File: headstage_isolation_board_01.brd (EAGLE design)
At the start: 50 x 40.9 mm, 49 parts

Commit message: fix some naming CONNECTOR STILL WRONG- DONT USE YET
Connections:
- net N$1 renamed MISO2+
- net N$14 renamed SCLK-
- net N$15 renamed SCLK+
- net N$16 renamed MOSI-
- net N$17 renamed MOSI+
- net N$18 renamed CS-
- net N$19 renamed CS+
- net N$2 renamed MISO2-
- net N$3 renamed MISO1+
- net N$4 renamed MISO1-
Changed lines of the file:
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@@
 <wire x1="64.77" y1="18.8595" x2="68.072" y2="12.446" width="0" layer="19" extent="1-1"/>
 </signal>
-<signal name="N$1">
+<signal name="MISO2+">
 <contactref element="S1" pad="T5"/>
 <contactref element="U$4" pad="P7"/>
@@
 <wire x1="58.166" y1="35.306" x2="56.5334" y2="35.306" width="0.2032" layer="1"/>
 </signal>
-<signal name="N$2">
+<signal name="MISO2-">
 <contactref element="S1" pad="B5"/>
 <contactref element="U$4" pad="P8"/>
@@
 <wire x1="66.04" y1="20.066" x2="66.04" y2="18.796" width="0.2032" layer="1"/>
 </signal>
-<signal name="N$3">
+<signal name="MISO1+">
 <contactref element="S1" pad="T4"/>
 <contactref element="U$4" pad="P6"/>
@@
 <wire x1="55.118" y1="34.036" x2="56.5334" y2="34.036" width="0.2032" layer="1"/>
 </signal>
-<signal name="N$4">
+<signal name="MISO1-">
 <contactref element="S1" pad="B4"/>
 <contactref element="U$4" pad="P5"/>
@@
 <wire x1="25.5905" y1="17.272" x2="25.527" y2="17.3355" width="0.2032" layer="1"/>
 </signal>
-<signal name="N$14">
+<signal name="SCLK-">
 <contactref element="S1" pad="B2"/>
 <contactref element="U$7" pad="P2"/>
@@
 <wire x1="64.8335" y1="16.256" x2="64.77" y2="16.3195" width="0.2032" layer="1"/>
 </signal>
-<signal name="N$15">
+<signal name="SCLK+">
 <contactref element="S1" pad="T2"/>
 <contactref element="U$7" pad="P1"/>
@@
 <wire x1="58.166" y1="19.304" x2="56.388" y2="21.082" width="0.2032" layer="1"/>
 </signal>
-<signal name="N$16">
+<signal name="MOSI-">
 <contactref element="S1" pad="B3"/>
 <contactref element="U$7" pad="P3"/>
@@
 <wire x1="64.77" y1="17.018" x2="64.77" y2="16.9545" width="0" layer="19" extent="1-1"/>
 </signal>
-<signal name="N$17">
+<signal name="MOSI+">
 <contactref element="S1" pad="T3"/>
 <contactref element="U$7" pad="P4"/>
@@
 <wire x1="57.912" y1="24.892" x2="56.388" y2="24.892" width="0.2032" layer="1"/>
 </signal>
-<signal name="N$18">
+<signal name="CS-">
 <contactref element="S1" pad="B1"/>
 <contactref element="U$8" pad="P3"/>
@@
 <wire x1="64.77" y1="14.986" x2="64.77" y2="15.6845" width="0.2032" layer="1"/>
 </signal>
-<signal name="N$19">
+<signal name="CS+">
 <contactref element="S1" pad="T1"/>
 <contactref element="U$8" pad="P4"/>

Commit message: added correct connector
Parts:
- added S3: RHD2000-CABLE-DAQ-SIDE, RHD2000_eval_board:OMNETICS_PZN-12-AA
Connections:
- net N$10 renamed MISO2-_ISOLATED
- net N$11 renamed MISO1+_ISOLATED
- net N$12 renamed MISO1-V
- net N$13 renamed MISO2+_ISOLATED
- net N$20 renamed CS-_ISOLATED
- net N$21 renamed SCLK-_ISOLATED
- net N$22 renamed SCLK+_ISOLATED
- net N$23 renamed MOSI-_ISOLATED
- net N$24 renamed MOSI+_ISOLATED
- net N$9 renamed CS+_ISOLATED
- new net CCS+: S3.B1
- new net CCS-: S3.T1
- new net CGND: S3.T6
- new net CMISO1+: S3.B4
- new net CMISO1-: S3.T4
- new net CMISO2+: S3.B5
- new net CMISO2-: S3.T5
- new net CMOSI+: S3.B3
- new net CMOSI-: S3.T3
- new net CSCLK+: S3.B2
- new net CSCLK-: S3.T2
- new net CVDD: S3.B6
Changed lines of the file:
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@@
 <layer number="14" name="Route14" color="1" fill="6" visible="no" active="yes"/>
 <layer number="15" name="Route15" color="4" fill="6" visible="no" active="yes"/>
-<layer number="16" name="Bottom" color="9" fill="1" visible="no" active="yes"/>
+<layer number="16" name="Bottom" color="9" fill="1" visible="yes" active="yes"/>
 <layer number="17" name="Pads" color="2" fill="1" visible="no" active="yes"/>
 <layer number="18" name="Vias" color="2" fill="1" visible="no" active="yes"/>
-<layer number="19" name="Unrouted" color="12" fill="1" visible="no" active="yes"/>
+<layer number="19" name="Unrouted" color="12" fill="1" visible="yes" active="yes"/>
 <layer number="20" name="Dimension" color="15" fill="1" visible="yes" active="yes"/>
 <layer number="21" name="tPlace" color="7" fill="1" visible="yes" active="yes"/>
@@
 <element name="C17" library="RHD2000_eval_board" package="0603" value="100n" x="52.07" y="27.178"/>
 <element name="C18" library="RHD2000_eval_board" package="0603" value="100n" x="51.054" y="39.116"/>
+<element name="S3" library="RHD2000_eval_board" package="OMNETICS_PZN-12-AA" value="RHD2000-CABLE-DAQ-SIDE" x="13.208" y="17.78" rot="R90"/>
 </elements>
 <signals>
@@
 <wire x1="37.084" y1="34.036" x2="36.188" y2="34.036" width="0.2032" layer="1"/>
 </signal>
-<signal name="N$10">
+<signal name="MISO2-_ISOLATED">
 <contactref element="S2" pad="B5"/>
 <contactref element="U$6" pad="P1"/>
@@
 <wire x1="27.178" y1="26.924" x2="27.178" y2="33.782" width="0.2032" layer="1"/>
 </signal>
-<signal name="N$11">
+<signal name="MISO1+_ISOLATED">
 <contactref element="U$6" pad="P3"/>
 <contactref element="S2" pad="T4"/>
@@
 <wire x1="32.258" y1="34.036" x2="30.988" y2="34.036" width="0.2032" layer="1"/>
 </signal>
-<signal name="N$12">
+<signal name="MISO1-V">
 <contactref element="U$6" pad="P4"/>
 <contactref element="S2" pad="B4"/>
@@
 <wire x1="28.702" y1="32.766" x2="30.988" y2="32.766" width="0.2032" layer="1"/>
 </signal>
-<signal name="N$13">
+<signal name="MISO2+_ISOLATED">
 <contactref element="S2" pad="T5"/>
 <contactref element="U$6" pad="P2"/>
@@
 <wire x1="62.9285" y1="14.986" x2="63.627" y2="15.6845" width="0.2032" layer="1"/>
 </signal>
-<signal name="N$9">
+<signal name="CS+_ISOLATED">
 <contactref element="S2" pad="T1"/>
 <contactref element="U$9" pad="P7"/>
@@
 <wire x1="31.496" y1="16.256" x2="30.868" y2="16.256" width="0" layer="19" extent="1-1"/>
 </signal>
-<signal name="N$20">
+<signal name="CS-_ISOLATED">
 <contactref element="S2" pad="B1"/>
 <contactref element="U$9" pad="P8"/>
@@
 <wire x1="37.084" y1="16.256" x2="36.068" y2="16.256" width="0.2032" layer="1"/>
 </signal>
-<signal name="N$21">
+<signal name="SCLK-_ISOLATED">
 <contactref element="S2" pad="B2"/>
 <contactref element="U$5" pad="P5"/>
@@
 <wire x1="24.3205" y1="19.304" x2="24.384" y2="19.2405" width="0.2032" layer="1"/>
 </signal>
-<signal name="N$22">
+<signal name="SCLK+_ISOLATED">
 <contactref element="U$5" pad="P6"/>
 <contactref element="S2" pad="T2"/>
@@
 <wire x1="25.5905" y1="19.304" x2="25.527" y2="19.2405" width="0.2032" layer="1"/>
 </signal>
-<signal name="N$23">
+<signal name="MOSI-_ISOLATED">
 <contactref element="U$5" pad="P8"/>
 <contactref element="S2" pad="B3"/>
@@
 <wire x1="23.9395" y1="18.542" x2="24.384" y2="18.6055" width="0.2032" layer="1"/>
 </signal>
-<signal name="N$24">
+<signal name="MOSI+_ISOLATED">
 <contactref element="U$5" pad="P7"/>
 <contactref element="S2" pad="T3"/>
@@
 <signal name="N$31">
 </signal>
+<signal name="CCS-">
+<contactref element="S3" pad="T1"/>
+</signal>
+<signal name="CCS+">
+<contactref element="S3" pad="B1"/>
+</signal>
+<signal name="CSCLK-">
+<contactref element="S3" pad="T2"/>
+</signal>
+<signal name="CSCLK+">
+<contactref element="S3" pad="B2"/>
+</signal>
+<signal name="CMOSI-">
+<contactref element="S3" pad="T3"/>
+</signal>
+<signal name="CMOSI+">
+<contactref element="S3" pad="B3"/>
+</signal>
+<signal name="CMISO1-">
+<contactref element="S3" pad="T4"/>
+</signal>
+<signal name="CMISO1+">
+<contactref element="S3" pad="B4"/>
+</signal>
+<signal name="CMISO2-">
+<contactref element="S3" pad="T5"/>
+</signal>
+<signal name="CMISO2+">
+<contactref element="S3" pad="B5"/>
+</signal>
+<signal name="CGND">
+<contactref element="S3" pad="T6"/>
+</signal>
+<signal name="CVDD">
+<contactref element="S3" pad="B6"/>
+</signal>
 </signals>

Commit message: routed correct headstage connector
and some other fixes.
Still lacking testpoints
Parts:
- removed S2: RHD2000-CABLE-AMP-SIDE, RHD2000:OMNETICS_PZN-12-AA
- moved S3 9.40 mm to (22.6, 17.5)
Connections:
- removed net CCS+: S3.B1
- removed net CCS-: S3.T1
- removed net CGND: S3.T6
- removed net CMISO1+: S3.B4
- removed net CMISO1-: S3.T4
- removed net CMISO2+: S3.B5
- removed net CMISO2-: S3.T5
- removed net CMOSI+: S3.B3
- removed net CMOSI-: S3.T3
- removed net CSCLK+: S3.B2
- removed net CSCLK-: S3.T2
- removed net CVDD: S3.B6
- removed net MISO1-V: S2.B4, U$6.P4
- new net MISO1-_ISOLATED: S3.T4, U$6.P4
- net CS+_ISOLATED: now also S3.B1; no longer S2.T1
- net CS-_ISOLATED: now also S3.T1; no longer S2.B1
- net GND_ISOLATED: now also S3.T6; no longer S2.B6
- net MISO1+_ISOLATED: now also S3.B4; no longer S2.T4
- net MISO2+_ISOLATED: now also S3.B5; no longer S2.T5
- net MISO2-_ISOLATED: now also S3.T5; no longer S2.B5
- net MOSI+_ISOLATED: now also S3.B3; no longer S2.T3
- net MOSI-_ISOLATED: now also S3.T3; no longer S2.B3
- net SCLK+_ISOLATED: now also S3.B2; no longer S2.T2
- net SCLK-_ISOLATED: now also S3.T2; no longer S2.B2
- net VDD_ISOLATED: now also S3.B6; no longer S2.T6
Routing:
- net MISO1-V: track 22.8 -> 0.00 mm
- net MISO1-_ISOLATED: track 0.00 -> 21.4 mm, vias 0 -> 2
- net GND_ISOLATED: track 50.3 -> 30.8 mm, vias 10 -> 2
- net GND: track 30.3 -> 41.6 mm, vias 3 -> 1
- net MOSI+_ISOLATED: track 8.00 -> 13.5 mm
- net CS-_ISOLATED: track 14.5 -> 9.36 mm, vias 2 -> 0
- net SCLK+_ISOLATED: track 8.38 -> 13.4 mm, vias 0 -> 2
- net CS+_ISOLATED: track 12.9 -> 10.3 mm, vias 2 -> 0
- net VDD_ISOLATED: track 47.6 -> 45.7 mm
- net MOSI-_ISOLATED: track 11.5 -> 9.71 mm
- net MISO2+_ISOLATED: track 27.2 -> 25.5 mm, vias 0 -> 2
- net 5V_ISOLATED: track 37.0 -> 38.0 mm
- net MISO2-_ISOLATED: track 26.8 -> 25.8 mm, vias 0 -> 2
- net SCLK-_ISOLATED: track 13.5 -> 12.7 mm, vias 0 -> 2
- net MISO1+_ISOLATED: track 23.3 -> 24.1 mm
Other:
- board size 50 x 40.9 mm -> 50 x 49.8 mm

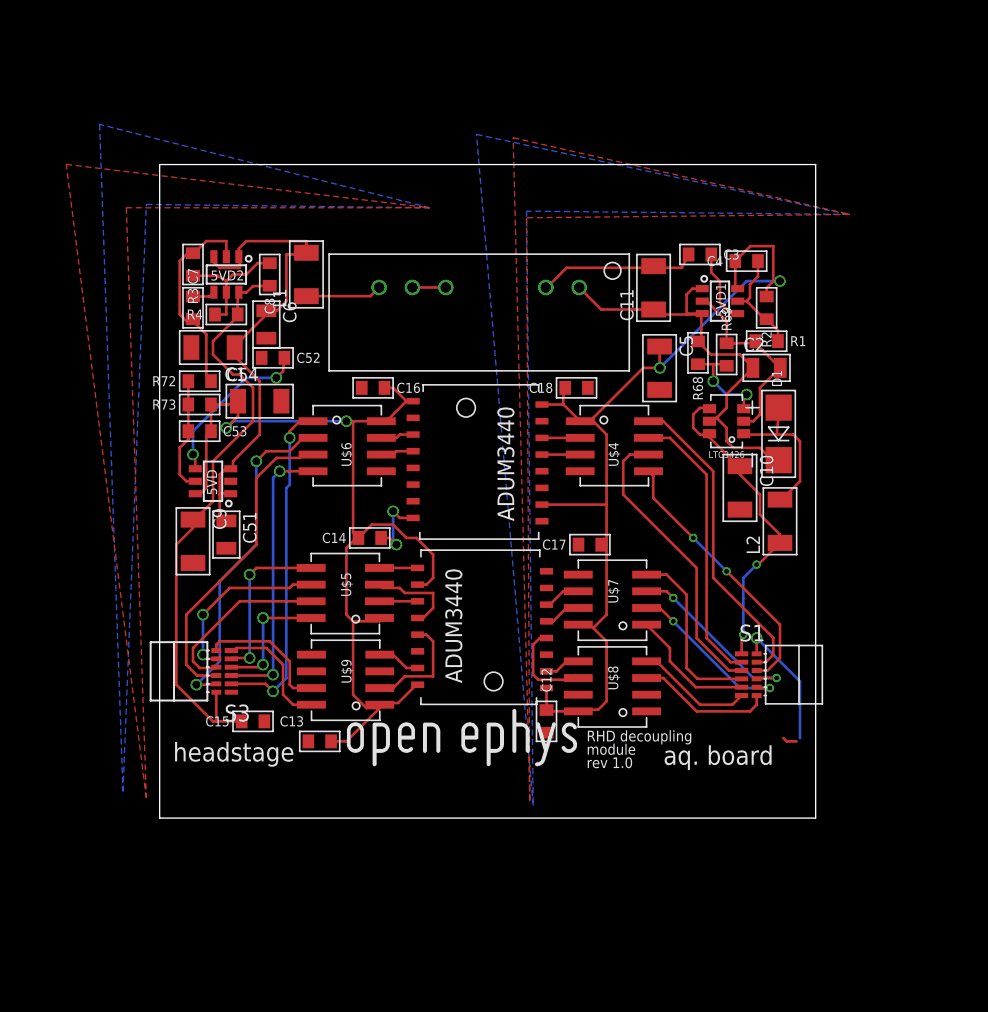
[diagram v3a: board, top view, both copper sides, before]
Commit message: partially added test points/ dc jack
can now choose between aq board power and external power jack, and
added a few test points
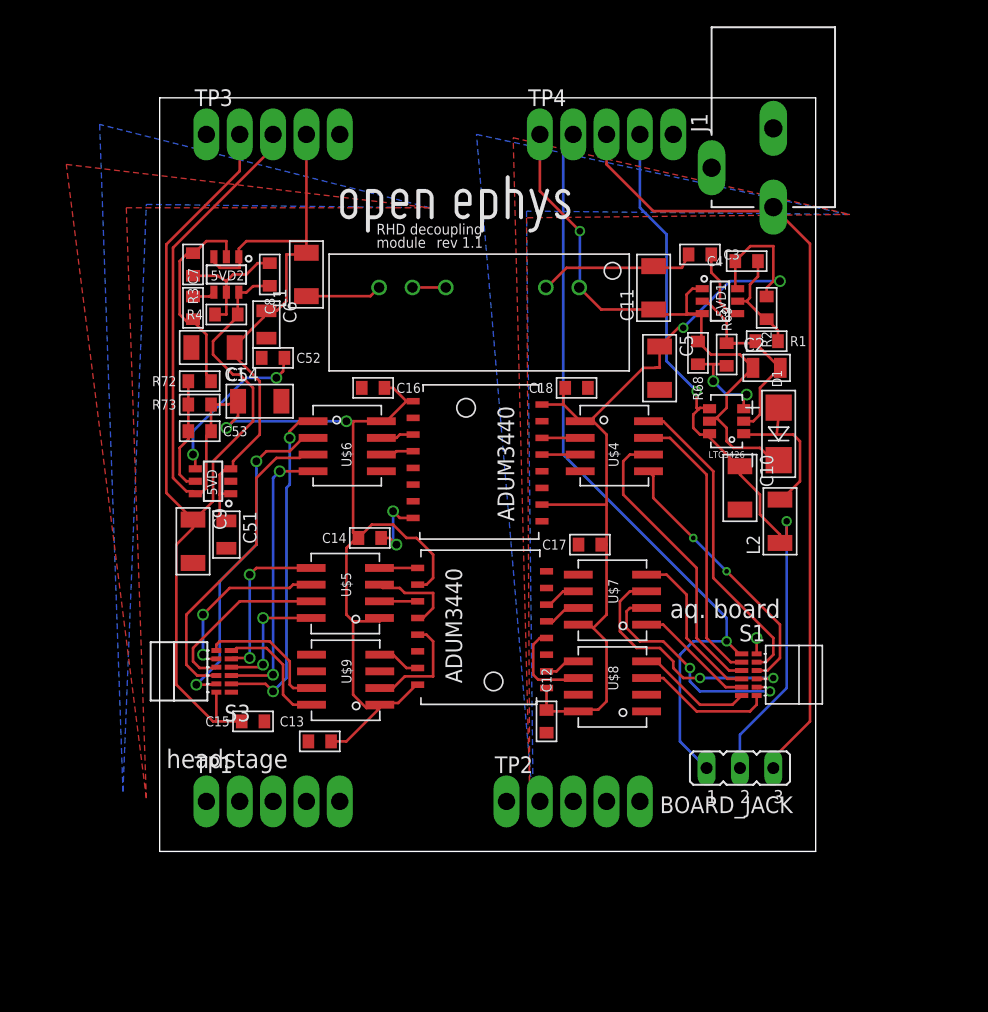
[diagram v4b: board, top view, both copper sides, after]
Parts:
- added BOARD_JACK: (no value), jumper:JP2
- added J1: DC_POWER_JACK-PJ-102AH, RHD2000_eval_board:PJ-102AH
- added TP1, TP2, TP3, TP4: TP5P5-25-13, testpad:P5-25-13
- moved U$1 40.6 mm to (32.4, 50.5)
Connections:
- new net N$9: TP3.TP-1
- new net PWR_JACK: BOARD_JACK.3, J1.1, TP4.TP-3
- new net VDD_FROM_BOARD: BOARD_JACK.1, S1.T6, TP4.TP-2
- net 5VBOOST: now also TP4.TP-1
- net 5V_ISOLATED: now also TP3.TP-4
- net GND: now also J1.2, J1.3, TP4.TP-5
- net GND_ISOLATED: now also TP3.TP-5
- net VDD33_ISOLATED: now also TP3.TP-3
- net VDD_IN: now also BOARD_JACK.2, TP4.TP-4; no longer S1.T6
- net VDD_ISOLATED: now also TP3.TP-2
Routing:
- net PWR_JACK: track 0.00 -> 61.6 mm
- net VDD_FROM_BOARD: track 0.00 -> 59.1 mm, vias 0 -> 1
- net VDD_IN: track 24.9 -> 59.6 mm
- net VDD_ISOLATED: track 45.7 -> 78.2 mm
- net VDD33_ISOLATED: track 74.4 -> 106.0 mm
- net 5VBOOST: track 33.8 -> 46.8 mm, vias 0 -> 1
- net GND: track 41.6 -> 31.5 mm
- net 5V_ISOLATED: track 38.0 -> 46.1 mm
- net MOSI-: track 14.2 -> 19.4 mm
- net SCLK-: track 13.0 -> 17.7 mm
- net MOSI+: track 13.8 -> 12.5 mm
- net VDD33: track 72.1 -> 71.4 mm
- net SCLK+: track 9.81 -> 9.21 mm
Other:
- board size 50 x 49.8 mm -> 50 x 57.4 mm
- board text added: "rev 1.1"
- board text removed: "rev 1.0"

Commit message: added all test points
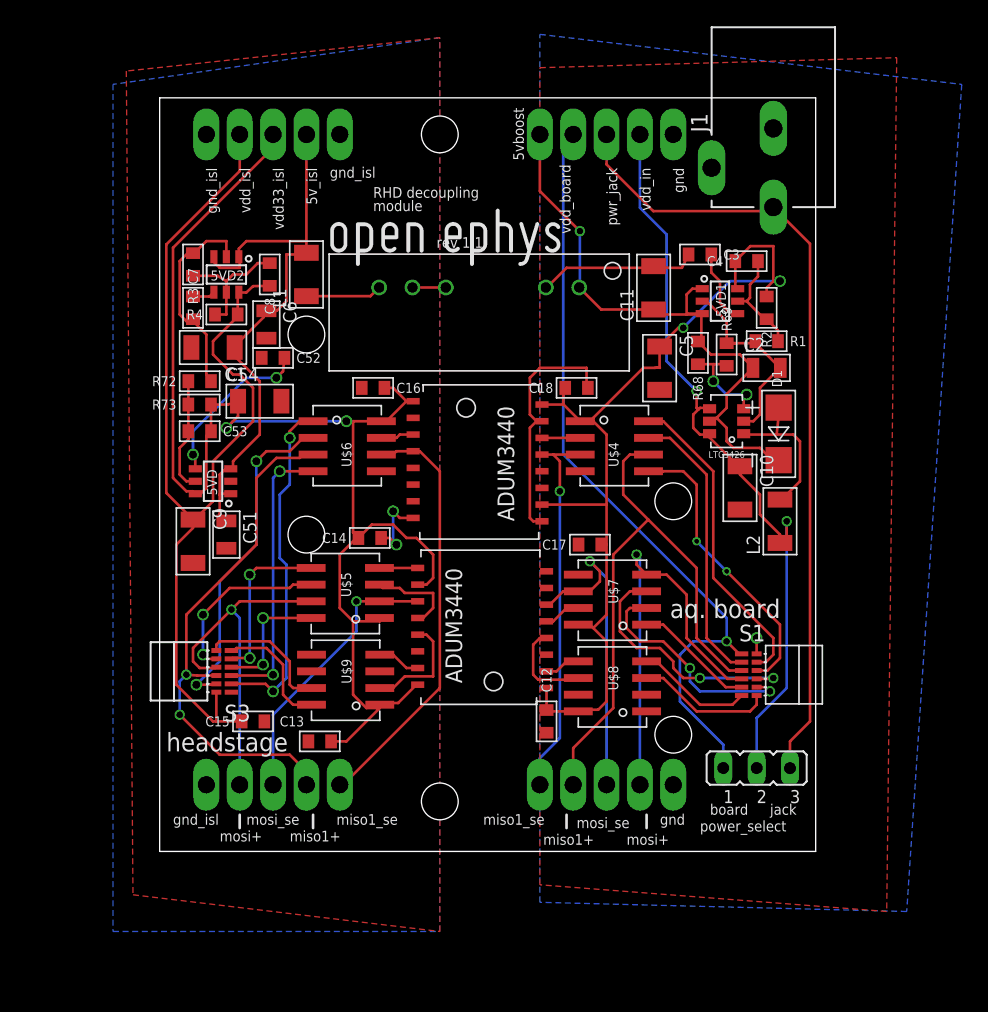
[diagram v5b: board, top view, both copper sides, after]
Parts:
- moved TP2 2.84 mm to (53.3, 8.89)
- moved U$1 2.65 mm to (31.6, 47.9)
- moved TP1 1.27 mm to (27.9, 8.89)
- moved BOARD_JACK 1.27 mm to (64.8, 10.2)
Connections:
- net N$26 renamed SCLK_SE
- net N$27 renamed CS_SE
- net N$29 renamed SCLK_ISOLATED_SE
- net N$30 renamed CS_ISOLATED_SE
- net N$5 renamed MISO2_SE
- net N$7 renamed MISO2_ISOLATED_SE
- removed net N$25: U$2.P6, U$7.P6
- removed net N$28: U$2.P11, U$5.P2
- removed net N$6: U$10.P13, U$4.P3
- removed net N$8: U$10.P4, U$6.P6
- removed net N$9: TP3.TP-1
- new net MISO1_ISOLATED_SE: TP1.TP-5, U$10.P4, U$6.P6
- new net MISO1_SE: TP2.TP-1, U$10.P13, U$4.P3
- new net MOSI_ISOLATED_SE: TP1.TP-3, U$2.P11, U$5.P2
- new net MOSI_SE: TP2.TP-3, U$2.P6, U$7.P6
- net GND: now also TP2.TP-5
- net GND_ISOLATED: now also TP1.TP-1, TP3.TP-1
- net MISO1+: now also TP2.TP-2
- net MISO1+_ISOLATED: now also TP1.TP-4
- net MOSI+: now also TP2.TP-4
- net MOSI+_ISOLATED: now also TP1.TP-2
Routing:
- net MISO1_ISOLATED_SE: track 0.00 -> 32.4 mm
- net MISO1_SE: track 0.00 -> 28.9 mm, vias 0 -> 1
- net MOSI_SE: track 0.00 -> 24.2 mm, vias 0 -> 1
- net MISO1+: track 22.4 -> 44.9 mm
- net MOSI_ISOLATED_SE: track 0.00 -> 21.3 mm, vias 0 -> 1
- net MOSI+: track 12.5 -> 31.9 mm, vias 0 -> 1
- net GND: track 31.5 -> 50.3 mm
- net MISO1+_ISOLATED: track 24.1 -> 40.3 mm, vias 0 -> 2
- net MOSI+_ISOLATED: track 13.5 -> 27.1 mm, vias 0 -> 1
- net N$6: track 2.91 -> 0.00 mm
- net N$28: track 2.91 -> 0.00 mm
- net N$25: track 2.84 -> 0.00 mm
- net N$8: track 2.53 -> 0.00 mm
- net MISO1-: track 20.5 -> 22.5 mm
- net VDD_FROM_BOARD: track 59.1 -> 59.6 mm
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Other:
- board text added: "5v_isl"
- board text added: "5vboost"
- board text added: "board"
- board text added: "gnd"
- board text added: "gnd_isl"
- board text added: "jack"
- board text added: "miso1+"
- board text added: "miso1_se"
- board text added: "mosi+"
- board text added: "mosi_se"
- board text added: "power_select"
- board text added: "pwr_jack"
- board text added: "vdd33_isl"
- board text added: "vdd_board"
- board text added: "vdd_in"
- board text added: "vdd_isl"

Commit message: added LVDS termination resistors
should fix bug #2
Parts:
- added R5, R6: 100, RHD2000_eval_board:0603
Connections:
- net MISO1+_ISOLATED: now also R6.1
- net MISO1-_ISOLATED: now also R6.2
- net MISO2+_ISOLATED: now also R5.1
- net MISO2-_ISOLATED: now also R5.2
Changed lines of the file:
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@@
 <attribute name="VALUE" x="53.34" y="11.049" size="1.27" layer="27" ratio="10"/>
 </element>
+<element name="R5" library="RHD2000_eval_board" package="0603" value="100" x="21.336" y="-3.556"/>
+<element name="R6" library="RHD2000_eval_board" package="0603" value="100" x="21.336" y="-5.588"/>
 </elements>
 <signals>
@@
 <wire x1="29.21" y1="35.814" x2="29.972" y2="36.576" width="0.2032" layer="1"/>
 <wire x1="29.972" y1="36.576" x2="30.988" y2="36.576" width="0.2032" layer="1"/>
+<contactref element="R5" pad="2"/>
+<wire x1="22.1996" y1="-3.556" x2="24.765" y2="16.5735" width="0" layer="19" extent="1-1"/>
 </signal>
 <signal name="MISO1+_ISOLATED">
@@
 <wire x1="20.828" y1="16.764" x2="21.336" y2="17.272" width="0.2032" layer="16"/>
 <via x="21.336" y="17.272" extent="1-16" drill="0.5"/>
+<contactref element="R6" pad="1"/>
+<wire x1="20.4724" y1="-5.588" x2="23.876" y2="11.176" width="0" layer="19" extent="1-1"/>
 </signal>
 <signal name="MISO1-_ISOLATED">
@@
 <via x="28.448" y="32.766" extent="1-16" drill="0.6"/>
 <wire x1="28.448" y1="32.766" x2="30.988" y2="32.766" width="0.2032" layer="1"/>
+<contactref element="R6" pad="2"/>
+<wire x1="22.1996" y1="-5.588" x2="24.765" y2="17.2085" width="0" layer="19" extent="1-1"/>
 </signal>
 <signal name="MISO2+_ISOLATED">
@@
 <wire x1="22.098" y1="16.51" x2="23.1775" y2="16.51" width="0.2032" layer="1"/>
 <wire x1="23.1775" y1="16.51" x2="23.622" y2="16.5735" width="0.2032" layer="1"/>
+<contactref element="R5" pad="1"/>
+<wire x1="20.4724" y1="-3.556" x2="22.098" y2="16.51" width="0" layer="19" extent="1-16"/>
 </signal>
 <signal name="SCLK-">
